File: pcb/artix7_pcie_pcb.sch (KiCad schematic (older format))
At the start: 0 parts

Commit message: worked on configuration
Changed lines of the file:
@@
 LIBS:wbraun_ic_lib
 LIBS:xilinx-artix7
+LIBS:FMC_connector-cache
 LIBS:artix7_pcie_pcb-cache
 EELAYER 25 0
@@
 $Descr A4 11693 8268
 encoding utf-8
-Sheet 1 7
+Sheet 1 10
 Title ""
 Date ""
@@
 F1 "FPGA_transceivers.sch" 60
 $EndSheet
+$Sheet
+S 3450 2200 950  1300
+U 562EA200
+F0 "MyriadRF IO" 60
+F1 "myriadRF_IO.sch" 60
+F2 "RF_CLK" I R 4400 2400 50
+F3 "TX_CLK" I R 4400 2600 50
+F4 "RX_CLK" I R 4400 2800 50
+$EndSheet
+$Sheet
+S 5000 900  1000 1000
+U 56341AF3
+F0 "FPGA Config" 50
+F1 "FPGA_Config.sch" 50
+$EndSheet
+$Sheet
+S 5100 3600 900  1100
+U 5634E8F5
+F0 "Clocking" 50
+F1 "clock_gen.sch" 50
+$EndSheet
 $EndSCHEMATC

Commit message: DDR routing test 1
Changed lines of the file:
@@
 $Descr A4 11693 8268
 encoding utf-8
-Sheet 1 12
+Sheet 1 13
 Title ""
 Date ""
@@
 Text Label 2500 1900 0    60   ~ 0
 PCIE_PERST
+$Sheet
+S 5050 5500 1250 900
+U 5665CB54
+F0 "FPGA Ground" 60
+F1 "FPGA_gnd.sch" 60
+$EndSheet
 $EndSCHEMATC

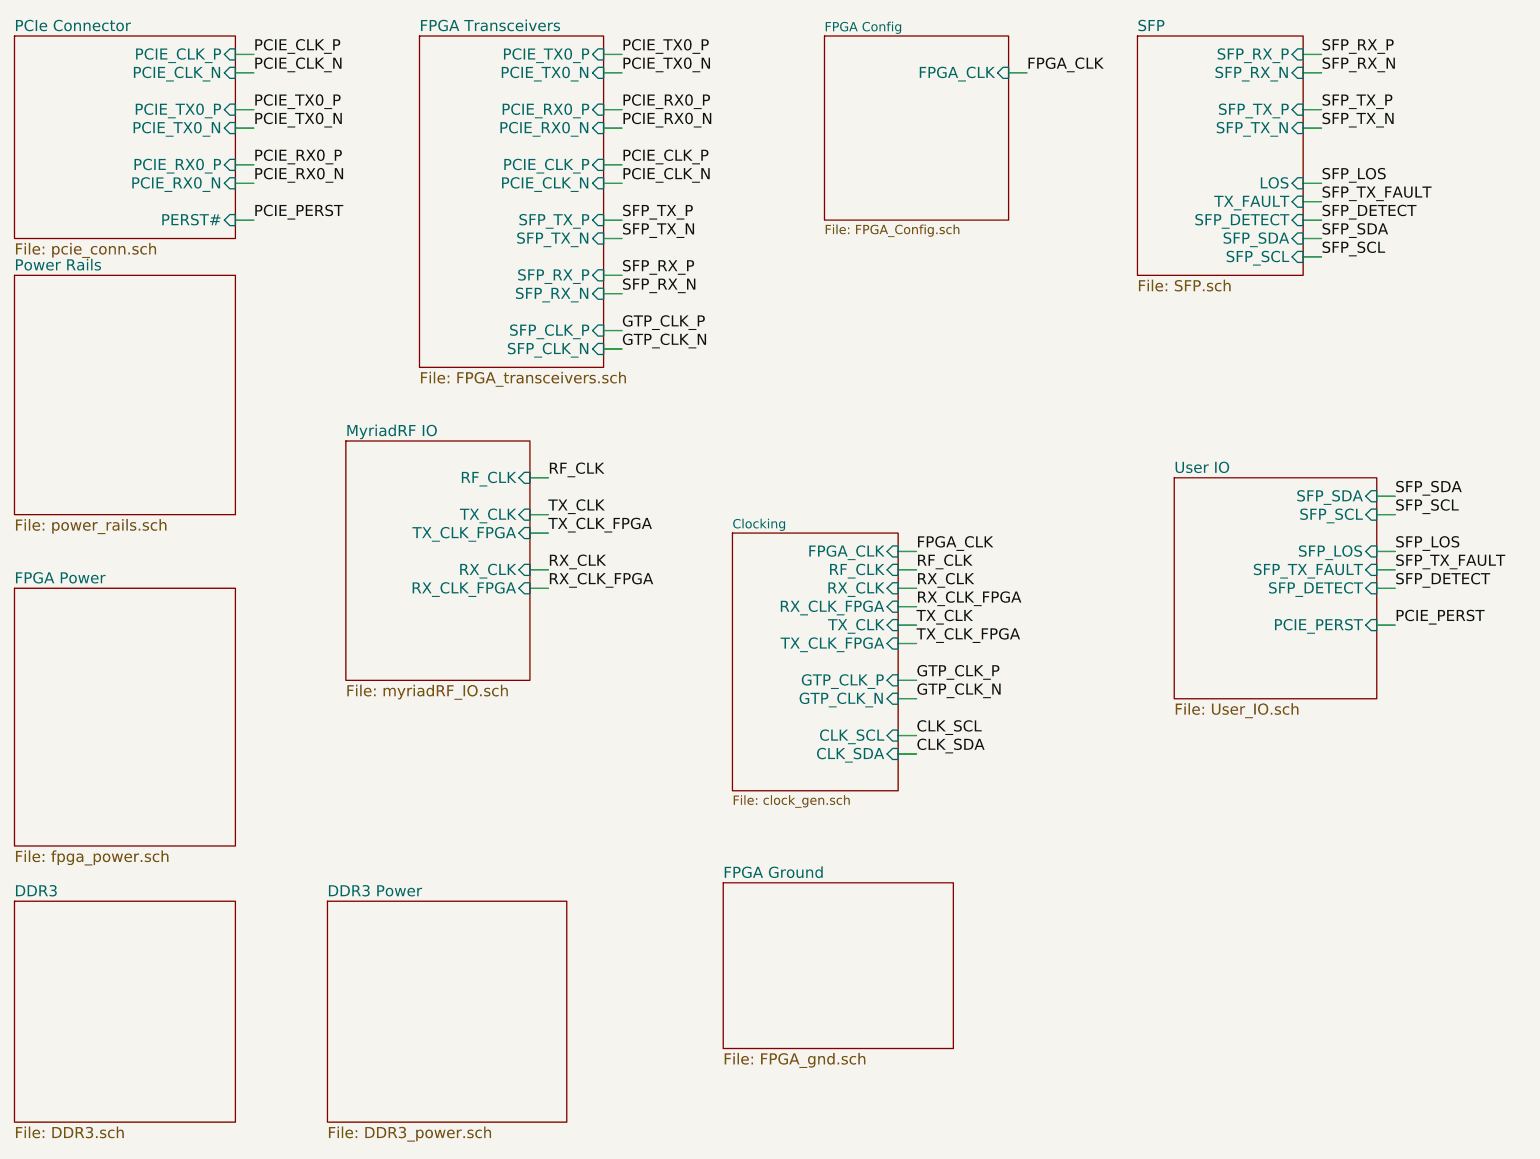
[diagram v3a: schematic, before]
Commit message: Finished most of the routing, removed DDR-3
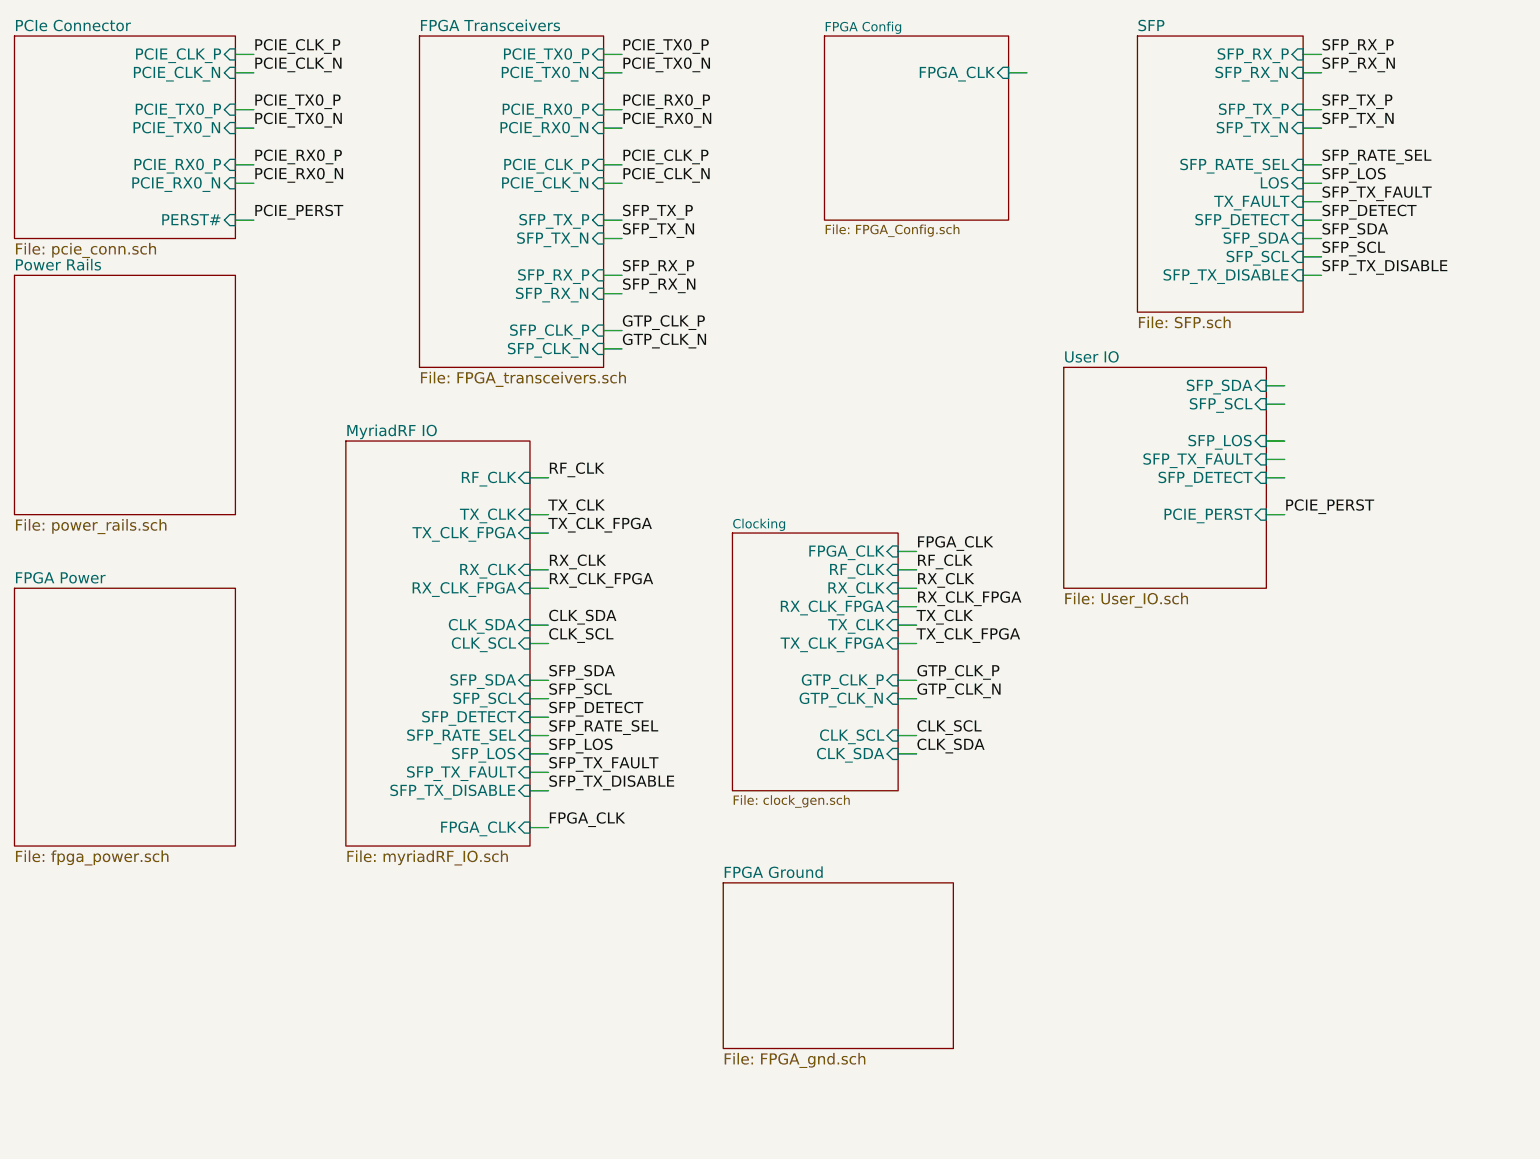
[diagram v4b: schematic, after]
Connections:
- net labels added: SFP_RATE_SEL, SFP_TX_DISABLE
- wire segments 50 -> 62
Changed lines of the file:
@@
 $Descr A4 11693 8268
 encoding utf-8
-Sheet 1 13
+Sheet 1 11
 Title ""
 Date ""
@@
 F0 "FPGA Power" 60
 F1 "fpga_power.sch" 60
-$EndSheet
-$Sheet
-S 1200 5600 1200 1200
-U 5618414C
-F0 "DDR3" 60
-F1 "DDR3.sch" 60
-$EndSheet
-$Sheet
-S 2900 5600 1300 1200
-U 56186E8C
-F0 "DDR3 Power" 60
-F1 "DDR3_power.sch" 60
 $EndSheet
 $Sheet
@@
 $EndSheet
 $Sheet
-S 3000 3100 1000 1300
+S 3000 3100 1000 2200
 U 562EA200
 F0 "MyriadRF IO" 60
@@
 F5 "TX_CLK_FPGA" I R 4000 3600 60
 F6 "RX_CLK_FPGA" I R 4000 3900 60
+F7 "CLK_SDA" I R 4000 4100 60
+F8 "CLK_SCL" I R 4000 4200 60
+F9 "SFP_SDA" I R 4000 4400 60
+F10 "SFP_SCL" I R 4000 4500 60
+F11 "SFP_DETECT" I R 4000 4600 60
+F12 "SFP_RATE_SEL" I R 4000 4700 60
+F13 "SFP_LOS" I R 4000 4800 60
+F14 "SFP_TX_FAULT" I R 4000 4900 60
+F15 "SFP_TX_DISABLE" I R 4000 5000 60
+F16 "FPGA_CLK" I R 4000 5200 60
 $EndSheet
 $Sheet
@@
 $EndSheet
 $Sheet
-S 7300 900  900  1300
+S 7300 900  900  1500
 U 56515F13
 F0 "SFP" 60
@@
 F9 "SFP_TX_P" I R 8200 1300 60
 F10 "SFP_TX_N" I R 8200 1400 60
-$EndSheet
-$Sheet
-S 7500 3300 1100 1200
+F11 "SFP_RATE_SEL" I R 8200 1600 60
+F12 "SFP_TX_DISABLE" I R 8200 2200 60
+$EndSheet
+$Sheet
+S 6900 2700 1100 1200
 U 565FB3DE
 F0 "User IO" 60
 F1 "User_IO.sch" 60
-F2 "SFP_SDA" I R 8600 3400 60
-F3 "SFP_SCL" I R 8600 3500 60
-F4 "SFP_LOS" I R 8600 3700 60
-F5 "SFP_TX_FAULT" I R 8600 3800 60
-F6 "SFP_DETECT" I R 8600 3900 60
-F7 "PCIE_PERST" I R 8600 4100 60
+F2 "SFP_SDA" I R 8000 2800 60
+F3 "SFP_SCL" I R 8000 2900 60
+F4 "SFP_LOS" I R 8000 3100 60
+F5 "SFP_TX_FAULT" I R 8000 3200 60
+F6 "SFP_DETECT" I R 8000 3300 60
+F7 "PCIE_PERST" I R 8000 3500 60
 $EndSheet
 Wire Wire Line
@@
 PCIE_CLK_N
 Wire Wire Line
-	8600 3400 8700 3400
-Wire Wire Line
-	8600 3500 8700 3500
-Wire Wire Line
-	8600 3700 8700 3700
-Wire Wire Line
-	8600 3800 8700 3800
-Wire Wire Line
-	8600 3900 8700 3900
-Text Label 8700 3400 0    60   ~ 0
+	8000 2800 8100 2800
+Wire Wire Line
+	8000 2900 8100 2900
+Wire Wire Line
+	8000 3100 8100 3100
+Wire Wire Line
+	8000 3200 8100 3200
+Wire Wire Line
+	8000 3300 8100 3300
+Text Label 4100 4400 0    60   ~ 0
 SFP_SDA
-Text Label 8700 3500 0    60   ~ 0
+Wire Wire Line
+	8200 2100 8300 2100
+Text Label 4100 4500 0    60   ~ 0
 SFP_SCL
-Text Label 8700 3700 0    60   ~ 0
+Text Label 4100 4800 0    60   ~ 0
 SFP_LOS
-Text Label 8700 3800 0    60   ~ 0
+Text Label 4100 4900 0    60   ~ 0
 SFP_TX_FAULT
-Text Label 8700 3900 0    60   ~ 0
+Text Label 4100 4600 0    60   ~ 0
 SFP_DETECT
-Text Label 8300 2000 0    60   ~ 0
-SFP_SDA
-Wire Wire Line
-	8200 2100 8300 2100
-Text Label 8300 2100 0    60   ~ 0
-SFP_SCL
-Text Label 8300 1700 0    60   ~ 0
-SFP_LOS
-Text Label 8300 1800 0    60   ~ 0
-SFP_TX_FAULT
-Text Label 8300 1900 0    60   ~ 0
-SFP_DETECT
-Text Label 6700 1100 0    60   ~ 0
-FPGA_CLK
-Wire Wire Line
-	8600 4100 8700 4100
-Text Label 8700 4100 0    60   ~ 0
+Wire Wire Line
+	8000 3500 8100 3500
+Text Label 8100 3500 0    60   ~ 0
 PCIE_PERST
 Text Label 2500 1900 0    60   ~ 0
@@
 F1 "FPGA_gnd.sch" 60
 $EndSheet
+Wire Wire Line
+	8200 1600 8300 1600
+Text Label 4100 4700 0    60   ~ 0
+SFP_RATE_SEL
+Wire Wire Line
+	4000 4100 4100 4100
+Wire Wire Line
+	4000 4200 4100 4200
+Wire Wire Line
+	4000 4400 4100 4400
+Wire Wire Line
+	4000 4500 4100 4500
+Wire Wire Line
+	4000 4600 4100 4600
+Wire Wire Line
+	4000 4700 4100 4700
+Wire Wire Line
+	4000 4800 4100 4800
+Wire Wire Line
+	4000 4900 4100 4900
+Text Label 4100 4200 0    60   ~ 0
+CLK_SCL
+Text Label 4100 4100 0    60   ~ 0
+CLK_SDA
+Wire Wire Line
+	8200 2200 8300 2200
+Wire Wire Line
+	4000 5000 4100 5000
+Wire Wire Line
+	4000 5200 4100 5200
+Text Label 4100 5000 0    60   ~ 0
+SFP_TX_DISABLE
+Text Label 4100 5200 0    60   ~ 0
+FPGA_CLK
+Text Label 8300 2000 0    60   ~ 0
+SFP_SDA
+Text Label 8300 2100 0    60   ~ 0
+SFP_SCL
+Text Label 8300 2200 0    60   ~ 0
+SFP_TX_DISABLE
+Text Label 8300 1900 0    60   ~ 0
+SFP_DETECT
+Text Label 8300 1800 0    60   ~ 0
+SFP_TX_FAULT
+Text Label 8300 1700 0    60   ~ 0
+SFP_LOS
+Text Label 8300 1600 0    60   ~ 0
+SFP_RATE_SEL
 $EndSCHEMATC

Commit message: Pending final check
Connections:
- wire segments 62 -> 61
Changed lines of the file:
@@
 F0 "FPGA Config" 50
 F1 "FPGA_Config.sch" 50
-F2 "FPGA_CLK" I R 6600 1100 60
 $EndSheet
 $Sheet
@@
 	2400 1900 2500 1900
 Wire Wire Line
-	6600 1100 6700 1100
-Wire Wire Line
 	8200 1000 8300 1000
